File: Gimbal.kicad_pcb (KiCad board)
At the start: 2 copper layers, 76.2 x 63.5 mm, 41 parts, among them J1 Conn_01x03, J2 USB_C_Receptacle_USB2.0, J3 0022232041, J4 0022232041, J5 0022232041, J6 Conn_01x02, Q1 Q_NPN_BCE, Q2 Q_NPN_BCE, SW1 SW_Push, U1 ESP32-S2-SOLO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

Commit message: prelim routing
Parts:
- added REF**: MountingHole_3.2mm_M3_DIN965_Pad, MountingHole:MountingHole_3.2mm_M3_DIN965_Pad, F.Cu at (177.8, 66.0)
- added REF**: MountingHole_3.2mm_M3_DIN965_Pad, MountingHole:MountingHole_3.2mm_M3_DIN965_Pad, F.Cu at (119.4, 119.4)
- moved C1 84.4 mm to (124.5, 104.1), turned to 90 degrees
- moved C4 84.4 mm to (124.5, 109.2)
- moved D2 74.7 mm to (119.4, 81.3)
- moved C5 68.3 mm to (165.1, 73.7), turned to -90 degrees
- moved C7 66.5 mm to (162.6, 73.7), turned to -90 degrees
- moved D3 66.2 mm to (124.5, 81.3)
- moved R1 62.0 mm to (129.5, 71.1)
- moved C8 61.5 mm to (167.6, 73.7), turned to -90 degrees
- moved R3 59.8 mm to (116.8, 90.8)
- moved R2 59.1 mm to (116.8, 86.6), turned to -90 degrees
- moved R9 58.3 mm to (166.4, 91.8), turned to 90 degrees
- moved D4 58.0 mm to (129.5, 81.3)
- moved J2 57.6 mm to (121.9, 68.6)
- moved J6 57.1 mm to (119.4, 99.8), turned to 180 degrees
- moved R6 56.2 mm to (139.2, 87.6), turned to -90 degrees
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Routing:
- net +3V3: track 0.00 -> 129.7 mm, vias 0 -> 2
- net +12V: track 0.00 -> 123.9 mm, vias 0 -> 4
- net /ESPRX: track 0.00 -> 52.9 mm, vias 0 -> 4
- net /ESPTX: track 0.00 -> 45.4 mm, vias 0 -> 2
- net /ESPIO2: track 0.00 -> 45.1 mm, vias 0 -> 2
- net /EN: track 0.00 -> 42.6 mm
- net /Motor2Step: track 0.00 -> 28.6 mm, vias 0 -> 2
- net /SPI_MISO: track 0.00 -> 28.1 mm, vias 0 -> 3
- net /Motor2Out1: track 0.00 -> 27.2 mm, vias 0 -> 2
- net Net-(J2-PadS1): track 0.00 -> 26.3 mm
- net /Motor2Dir: track 0.00 -> 26.1 mm, vias 0 -> 2
- net /VBUS: track 0.00 -> 24.3 mm, vias 0 -> 2
- net /ESPIO35: track 0.00 -> 23.6 mm
- net /ESPIO34: track 0.00 -> 23.4 mm, vias 0 -> 2
- net /Motor2M0: track 0.00 -> 22.3 mm
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- added copper zone on B.Cu, net GND
- added copper zone on F.Cu, net GND
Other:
- board size 76.2 x 63.5 mm -> 68.6 x 63.5 mm

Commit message: routing actually good
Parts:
- J2: footprint Connector_USB:USB_C_Receptacle_Amphenol_12401548E4-2A -> Connector_USB:USB_C_Receptacle_Amphenol_12401610E4-2A
- J5: footprint Connector_PinHeader_1.00mm:PinHeader_1x04_P1.00mm_Horizontal -> Connector_PinHeader_2.00mm:PinHeader_1x04_P2.00mm_Horizontal
- J6: footprint Connector_PinHeader_1.00mm:PinHeader_1x02_P1.00mm_Horizontal -> Connector_PinHeader_2.00mm:PinHeader_1x02_P2.00mm_Horizontal
- moved R4 5.24 mm to (156.2, 68.4), turned to -90 degrees
- moved C4 5.00 mm to (126.5, 104.6), turned to 90 degrees
- moved J5 4.76 mm to (117.9, 111.2)
- moved R1 4.71 mm to (127.0, 75.1)
- moved D5 3.87 mm to (153.7, 68.4), turned to -90 degrees
- moved R10 3.56 mm to (161.4, 101.6)
- moved R7 3.56 mm to (161.4, 118.1), turned to 180 degrees
- moved U5 3.56 mm to (159.0, 111.8)
- moved U6 3.56 mm to (159.0, 96.5)
- moved C11 3.56 mm to (157.0, 101.6)
- moved C6 3.56 mm to (157.0, 118.1)
- moved R8 3.56 mm to (163.1, 106.1)
- moved R9 2.79 mm to (163.6, 91.8)
- moved C10 2.54 mm to (165.5, 81.2)
- moved C7 2.54 mm to (160.5, 75.2)
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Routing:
- net GND: track 3.25 -> 105.8 mm, vias 0 -> 18
- net /EN: track 42.6 -> 72.0 mm, vias 0 -> 4
- net +3V3: track 129.7 -> 156.0 mm, vias 2 -> 11
- net Net-(D3-Pad2): track 14.1 -> 37.4 mm, vias 2 -> 6
- net /VBUS: track 24.3 -> 43.0 mm, vias 2 -> 4
- net /ESPIO35: track 23.6 -> 41.5 mm, vias 0 -> 6
- net /SPI_CLK: track 14.3 -> 28.8 mm, vias 0 -> 4
- net Net-(D4-Pad2): track 9.04 -> 23.1 mm, vias 0 -> 3
- net Net-(R8-Pad1): track 5.12 -> 17.4 mm, vias 0 -> 2
- net /ESPIO2: track 45.1 -> 56.1 mm, vias 2 -> 4
- net /ESPRX: track 52.9 -> 44.1 mm
- net /ESPIO0: track 9.84 -> 18.5 mm, vias 0 -> 2
- net Net-(Q1-Pad1): track 14.7 -> 23.0 mm, vias 0 -> 2
- net Net-(R9-Pad1): track 0.00 -> 7.51 mm, vias 0 -> 2
- net /Motor2Out4: track 14.2 -> 20.5 mm
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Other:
- board text added: "12V"
- board text added: "3.3V"
- board text added: "GIMBALL PROJECT"
- board text added: "GND"
- board text added: "RX TX"
- board text added: "Vin"

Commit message: new schematic
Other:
- board text added: "GIMBAL PROJECT"
- board text removed: "GIMBALL PROJECT"
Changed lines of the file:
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@@
     (effects (font (size 1 1) (thickness 0.15)))
   )
-  (gr_text "GIMBALL PROJECT" (at 141.224 72.644) (layer "F.SilkS")
+  (gr_text "GIMBAL PROJECT" (at 141.224 72.644) (layer "F.SilkS")
     (effects (font (size 1.5 1.5) (thickness 0.3)))
   )

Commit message: started new layout
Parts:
- removed D3, D4: DIODE, Package_TO_SOT_SMD:SOT-143
- removed Q1, Q2: Q_NPN_BCE, Package_TO_SOT_SMD:TSOT-23
- removed R6: 10k, Resistor_SMD:R_0805_2012Metric
- removed REF** (x2): MountingHole_3.2mm_M3_DIN965_Pad, MountingHole:MountingHole_3.2mm_M3_DIN965_Pad
- added C12: 15uF, Capacitor_SMD:C_0805_2012Metric, F.Cu at (150.9, 70.4)
- added C13: 15uF, Capacitor_SMD:C_0805_2012Metric, F.Cu at (148.3, 70.4)
- added C14: 15uF, Capacitor_SMD:C_0805_2012Metric, F.Cu at (145.5, 70.4)
- added C15: 0.47 uF, Capacitor_SMD:C_0805_2012Metric, F.Cu at (142.7, 70.4)
- added C16: .01uF, Capacitor_SMD:C_0805_2012Metric, F.Cu at (150.9, 76.5)
- added C17: 180uF, Capacitor_THT:CP_Radial_D8.0mm_P5.00mm, F.Cu at (127.0, 83.8)
- added C18: 180uF, Capacitor_THT:CP_Radial_D8.0mm_P5.00mm, F.Cu at (121.9, 83.8)
- added C19: 0.1uF, Capacitor_SMD:C_0805_2012Metric, F.Cu at (118.6, 93.5)
- added L1: 22uH, Inductor_SMD:L_10.4x10.4_H4.8, F.Cu at (161.6, 88.9)
- added SW2: SW_Push, Button_Switch_SMD:SW_Push_1P1T_NO_CK_KMR2, F.Cu at (119.4, 99.1)
- D2: footprint Package_TO_SOT_SMD:SOT-143 -> Diode_SMD:D_SMC
- J1: value Conn_01x03 -> XT60-M; footprint Connector_Molex:Molex_Micro-Fit_3.0_43650-0300_1x03_P3.00mm_Horizontal -> GIMBAL:AMASS_XT60-M
- J5: footprint Connector_PinHeader_2.00mm:PinHeader_1x04_P2.00mm_Horizontal -> Connector_PinHeader_2.00mm:PinHeader_1x04_P2.00mm_Vertical
- J6: footprint Connector_PinHeader_2.00mm:PinHeader_1x02_P2.00mm_Horizontal -> Connector_PinHeader_2.00mm:PinHeader_1x02_P2.00mm_Vertical
- R2: value 22.1k -> 5.6k
- R3: value 47.5k -> 10k
- U3: value CP2102N-Axx-xQFN28 -> LM2679SX-12; footprint Package_DFN_QFN:QFN-28-1EP_5x5mm_P0.5mm_EP3.35x3.35mm -> Package_TO_SOT_SMD:TO-263-7_TabPin8
- moved D2 57.9 mm to (175.3, 66.0), turned to 180 degrees
- moved R2 52.5 mm to (168.4, 76.7), turned to 90 degrees
- moved U3 38.6 mm to (159.8, 71.1), turned to 90 degrees
- moved SW1 36.0 mm to (124.5, 99.1), turned to 90 degrees
- moved C2 33.2 mm to (124.5, 94.0), turned to -90 degrees
- moved C3 26.4 mm to (137.2, 76.4)
- moved C5 26.4 mm to (137.2, 70.4)
- moved C8 26.4 mm to (139.7, 70.4)
- moved C9 26.4 mm to (134.5, 76.4)
- moved C10 26.4 mm to (139.6, 76.4)
- moved C7 26.4 mm to (134.6, 70.4)
- moved R4 19.5 mm to (137.2, 64.4)
- moved U4 19.5 mm to (143.5, 64.5)
- moved D5 19.5 mm to (134.6, 64.3)
- moved R5 17.7 mm to (125.2, 89.9), turned to 180 degrees
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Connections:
- D1 pad 1: +12V -> +BATT
- D2 pad 2: /VBUS -> Net-(C16-Pad2)
- J2 pad A4: /VBUS -> unconnected-(J2-PadA4)
- J2 pad A6: Net-(D4-Pad2) -> /D+
- J2 pad A7: Net-(D3-Pad2) -> /D-
- J2 pad A9: /VBUS -> unconnected-(J2-PadA4)
- J2 pad B4: /VBUS -> unconnected-(J2-PadA4)
- J2 pad B6: Net-(D4-Pad2) -> /D+
- J2 pad B7: Net-(D3-Pad2) -> /D-
- J2 pad B9: /VBUS -> unconnected-(J2-PadA4)
- R2 pad 1: /VBUS -> GND
- R3 pad 1: Net-(R2-Pad2) -> +3V3
- R3 pad 2: GND -> /EN
- R5 pad 1: /!RTS -> +3V3
- R5 pad 2: Net-(Q1-Pad1) -> /GPIO0
- U1 pad 10: /Motor1Dir -> unconnected-(U1-Pad10)
- U1 pad 11: /Motor1Step -> unconnected-(U1-Pad11)
- U1 pad 12: unconnected-(U1-Pad12) -> /Motor1Step
- U1 pad 13: /Motor2M1 -> /D-
- U1 pad 14: /Motor2M0 -> /D+
- U1 pad 17: unconnected-(U1-Pad17) -> /Motor2M1
- U1 pad 18: unconnected-(U1-Pad18) -> /Motor2M0
- U1 pad 19: unconnected-(U1-Pad19) -> /Motor2Dir
- U1 pad 23: /Motor2Dir -> unconnected-(U1-Pad23)
- U1 pad 24: /Motor2Step -> unconnected-(U1-Pad24)
- U1 pad 5: unconnected-(U1-Pad5) -> /Motor1M1
- U1 pad 6: unconnected-(U1-Pad6) -> /Motor1M0
- U1 pad 7: unconnected-(U1-Pad7) -> /Motor1Dir
- U1 pad 8: /Motor1M1 -> /Motor2Step
- U1 pad 9: /Motor1M0 -> unconnected-(U1-Pad9)
- U3 pad 1: unconnected-(U3-Pad1) -> Net-(C16-Pad2)
- U3 pad 2: unconnected-(U3-Pad2) -> +BATT
- U3 pad 3: GND -> /BUCKCB
- U3 pad 4: Net-(D4-Pad2) -> GND
- U3 pad 5: Net-(D3-Pad2) -> Net-(R2-Pad2)
- U3 pad 6: +3V3 -> +12V
- U3 pad 7: /VBUS -> unconnected-(U3-Pad7)
- U3 pad 8: Net-(R2-Pad2) -> (no net)
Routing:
- net +3V3: track 156.0 -> 32.9 mm, vias 11 -> 2
- net GND: track 105.8 -> 17.9 mm, vias 18 -> 2
- net /EN: track 72.0 -> 11.7 mm, vias 4 -> 0
- net /ESPIO2: track 56.1 -> 0.00 mm, vias 4 -> 0
- net /ESPTX: track 46.2 -> 0.00 mm, vias 5 -> 0
- net /ESPRX: track 44.1 -> 0.00 mm, vias 4 -> 0
- net /VBUS: track 43.0 -> 0.00 mm, vias 4 -> 0
- net /ESPIO35: track 41.5 -> 0.00 mm, vias 6 -> 0
- net Net-(D3-Pad2): track 37.4 -> 0.00 mm, vias 6 -> 0
- net /SPI_MISO: track 33.3 -> 0.00 mm, vias 8 -> 0
- net +BATT: track 0.00 -> 32.6 mm
- net /Motor2Step: track 32.2 -> 0.00 mm, vias 4 -> 0
- net /SPI_CLK: track 28.8 -> 0.00 mm, vias 4 -> 0
- net Net-(C16-Pad2): track 0.00 -> 28.8 mm, vias 0 -> 4
- net /ESPIO34: track 27.1 -> 0.00 mm, vias 4 -> 0
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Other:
- board text removed: "GIMBAL PROJECT"

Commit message: New layout
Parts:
- moved U2 8.64 mm to (141.2, 88.9)
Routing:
- net +3V3: track 32.9 -> 162.0 mm, vias 2 -> 17
- net +12V: track 106.3 -> 170.1 mm, vias 11 -> 13
- net /EN: track 11.7 -> 69.9 mm, vias 0 -> 4
- net /D-: track 2.01 -> 59.0 mm, vias 0 -> 4
- net /D+: track 5.52 -> 61.3 mm, vias 2 -> 4
- net GND: track 17.9 -> 66.7 mm, vias 2 -> 10
- net /ESPIO2: track 0.00 -> 48.8 mm, vias 0 -> 6
- net /ESPRX: track 0.00 -> 47.4 mm, vias 0 -> 4
- net /ESPIO35: track 0.00 -> 34.8 mm, vias 0 -> 6
- net /ESPIO4: track 0.00 -> 32.1 mm, vias 0 -> 2
- net /Motor2Dir: track 0.00 -> 29.2 mm, vias 0 -> 4
- net Net-(C16-Pad2): track 28.8 -> 54.8 mm, vias 4 -> 6
- net /Motor2M0: track 0.00 -> 25.7 mm, vias 0 -> 4
- net /Motor1Out1: track 0.00 -> 24.3 mm, vias 0 -> 2
- net /SPI_MISO: track 0.00 -> 22.5 mm, vias 0 -> 2
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
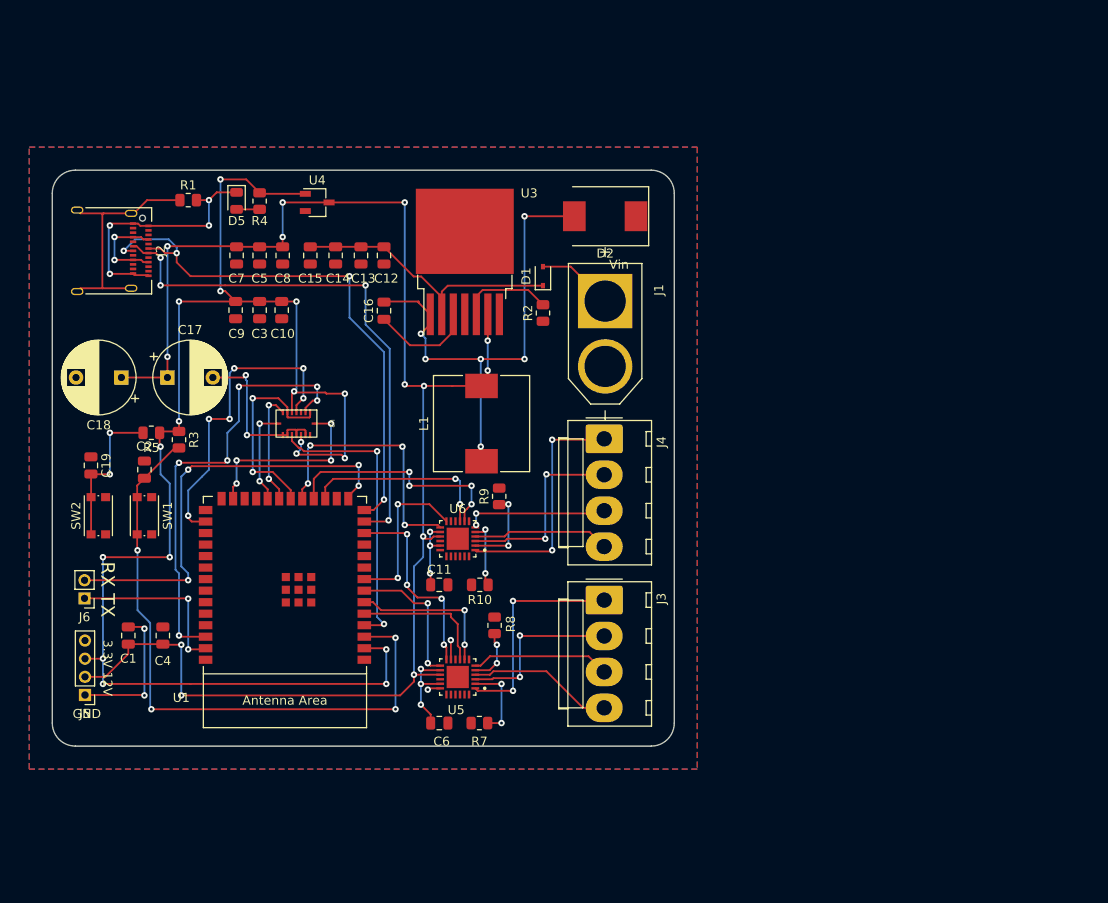
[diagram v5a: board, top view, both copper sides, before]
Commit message: updated layout and schematic to fix errors
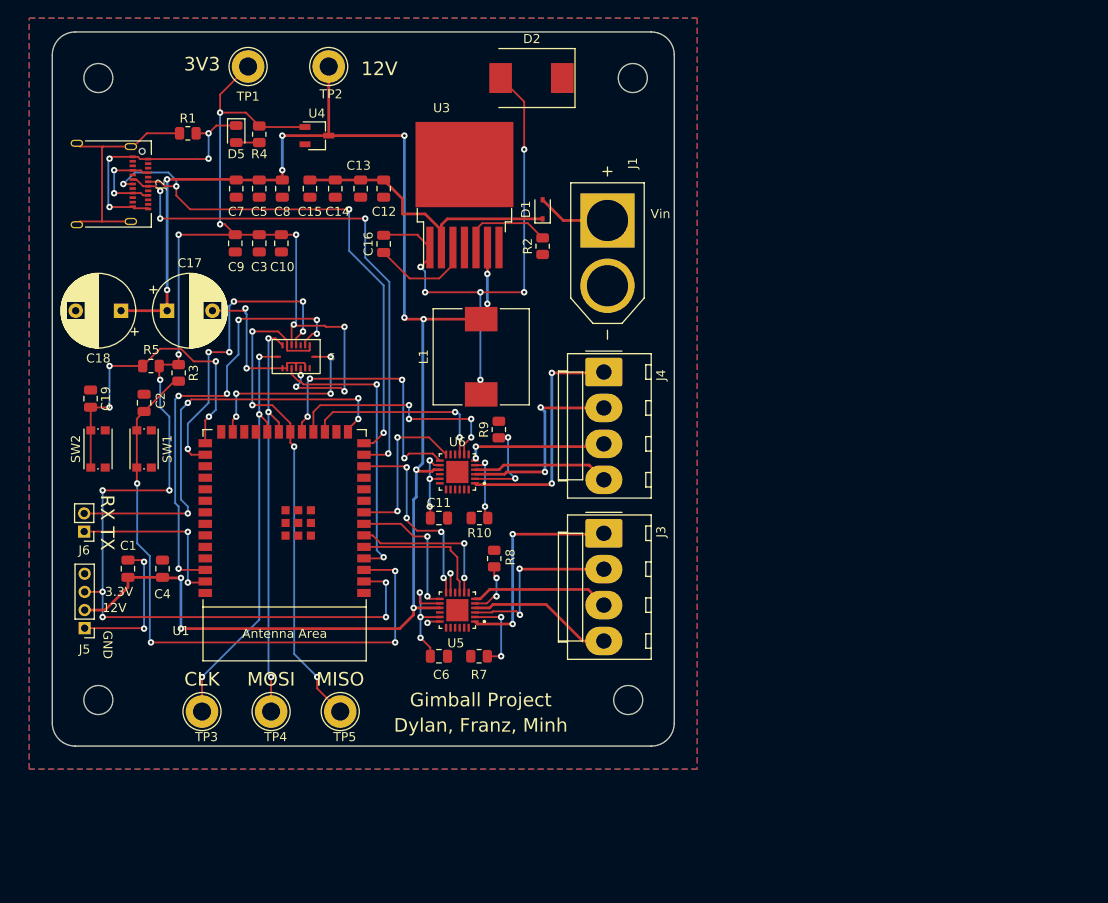
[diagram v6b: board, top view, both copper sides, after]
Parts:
- added REF**: MountingHole_3.2mm_M3, MountingHole:MountingHole_3.2mm_M3, F.Cu at (177.8, 119.4)
- added REF**: MountingHole_3.2mm_M3, MountingHole:MountingHole_3.2mm_M3, F.Cu at (178.3, 50.8)
- added REF**: MountingHole_3.2mm_M3, MountingHole:MountingHole_3.2mm_M3, F.Cu at (119.4, 119.4)
- added REF**: MountingHole_3.2mm_M3, MountingHole:MountingHole_3.2mm_M3, F.Cu at (119.4, 50.8)
- added TP1: TestPoint, TestPoint:TestPoint_Loop_D3.80mm_Drill2.0mm, F.Cu at (135.9, 49.5)
- added TP2: TestPoint, TestPoint:TestPoint_Loop_D3.80mm_Drill2.0mm, F.Cu at (144.8, 49.5)
- added TP3: TestPoint, TestPoint:TestPoint_Loop_D3.80mm_Drill2.0mm, F.Cu at (130.8, 120.7)
- added TP4: TestPoint, TestPoint:TestPoint_Loop_D3.80mm_Drill2.0mm, F.Cu at (138.4, 120.7)
- added TP5: TestPoint, TestPoint:TestPoint_Loop_D3.80mm_Drill2.0mm, F.Cu at (146.1, 120.7)
- moved D2 17.3 mm to (167.1, 50.8)
- moved J1 8.89 mm to (175.5, 70.1)
- moved C11 7.37 mm to (156.9, 99.3)
- moved R10 7.37 mm to (161.4, 99.3)
- moved U1 7.37 mm to (139.9, 99.3)
- moved C12 7.37 mm to (150.8, 63.0)
- moved C13 7.37 mm to (148.3, 63.0)
- moved C14 7.37 mm to (145.5, 63.0)
- moved C15 7.37 mm to (142.7, 63.0)
- moved C5 7.37 mm to (137.1, 63.0)
- moved C7 7.37 mm to (134.6, 63.0)
- moved C8 7.37 mm to (139.7, 63.0)
- moved D5 7.37 mm to (134.6, 57.0)
- moved U4 7.37 mm to (143.5, 57.1)
- moved C1 7.37 mm to (122.6, 104.9)
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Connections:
- C19 pad 2: /GPIO0 -> /ESPIO0
- R5 pad 2: /GPIO0 -> /ESPIO0
- SW2 pad 1: /GPIO0 -> /ESPIO0
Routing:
- net /ESPIO0: track 0.00 -> 35.9 mm, vias 0 -> 4
- net /SPI_CLK: track 10.7 -> 46.1 mm, vias 2 -> 3
- net /SPI_MOSI: track 12.7 -> 45.8 mm, vias 2 -> 3
- net /SPI_MISO: track 22.5 -> 55.6 mm, vias 2 -> 4
- net /GPIO0: track 17.0 -> 0.00 mm, vias 2 -> 0
- net +12V: track 170.1 -> 178.4 mm
- net +3V3: track 162.0 -> 168.4 mm
- net Net-(C16-Pad2): track 54.8 -> 58.3 mm
- net Net-(C6-Pad1): track 10.8 -> 13.0 mm
- net Net-(R9-Pad1): track 9.27 -> 10.4 mm
- net +BATT: track 32.6 -> 33.6 mm
- net /Motor2Out2: track 21.4 -> 22.1 mm
- net Net-(C11-Pad1): track 8.11 -> 8.82 mm
- net /Motor1Out2: track 18.7 -> 19.4 mm
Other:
- board size 68.6 x 63.5 mm -> 68.6 x 78.7 mm
- board text added: "3V3"
- board text added: "CLK"
- board text added: "Dylan, Franz, Minh"
- board text added: "Gimball Project"
- board text added: "MISO"
- board text added: "MOSI"

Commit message: layout completed
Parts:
- removed D5: LED, LED_SMD:LED_0805_2012Metric
- removed R10: 500m, Resistor_SMD:R_0805_2012Metric
- removed REF** (x4): MountingHole_3.2mm_M3, MountingHole:MountingHole_3.2mm_M3
- added D3: LED, LED_SMD:LED_0805_2012Metric, F.Cu at (134.6, 57.1)
- added R6: 500m, Resistor_SMD:R_0805_2012Metric, F.Cu at (163.1, 100.1)
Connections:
- J2 pad A4: unconnected-(J2-PadA4) -> GND
- J2 pad A9: unconnected-(J2-PadA4) -> GND
- J2 pad B4: unconnected-(J2-PadA4) -> GND
- J2 pad B9: unconnected-(J2-PadA4) -> GND
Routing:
- net unconnected-(J2-PadA4): track 10.3 -> 0.00 mm, vias 2 -> 0
- net GND: track 66.7 -> 76.6 mm

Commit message: comment
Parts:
- added R10: 10k, Resistor_SMD:R_0805_2012Metric, F.Cu at (120.4, 54.0)
- added R11: 10k, Resistor_SMD:R_0805_2012Metric, F.Cu at (124.6, 54.0)
